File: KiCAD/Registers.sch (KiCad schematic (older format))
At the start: 25 parts, among them U701 74HCT138N, U704 74LS27, U705 74HCT32N, U706 74HCT574N, U707 74HCT574N, U708 74HCT574N, U712 74LS27, U713 74HCT32N, U714 74HCT574N, U715 74HCT574N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

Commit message: Moved SP out of register module into SP module; changed RS0 assert signal alias from RS0 to RSH; moved uCode and program code to different subdirs of Programming/ .
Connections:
- net REG_ASSERT_RS0 renamed RSH
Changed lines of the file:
@@
 $EndComp
 Text HLabel 1400 5050 0    50   Input ~ 0
-REG_ASSERT_RS0
+RSH
 Wire Wire Line
 	1400 4725 1450 4725

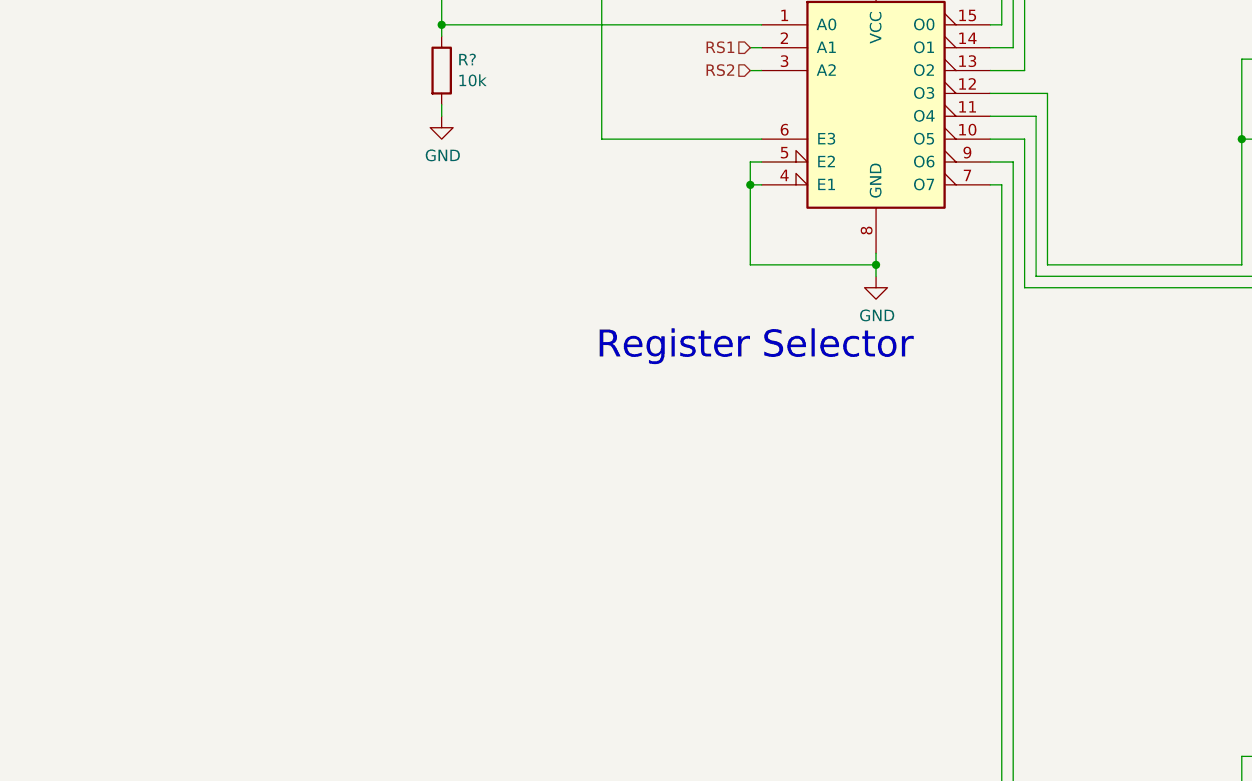
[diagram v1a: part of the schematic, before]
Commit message: First working versiongit add .  Added CSU control signal for updating C and O flags during add operations only.  Added circuitry to disable the reg decoder unless ~RI or ~RO are asserted.  Potential future issues: PC clock noise, reg clock noise, clock module being crap..
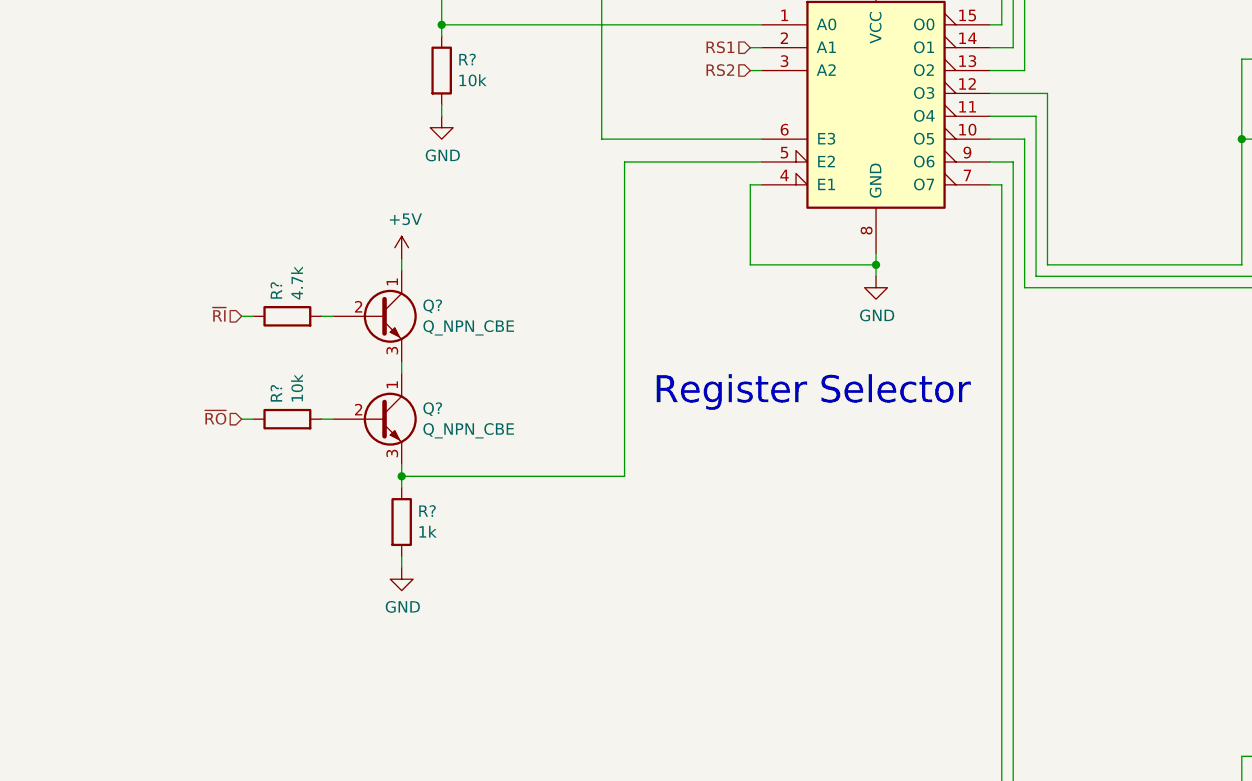
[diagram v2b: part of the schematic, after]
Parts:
- added Q? (x2): Q_NPN_CBE, symbol Breadboard_CPU-rescue:Q_NPN_CBE-Device
- added R?: 4.7k, symbol Breadboard_CPU-rescue:R-Device
- added R?: 10k, symbol Breadboard_CPU-rescue:R-Device
- added R?: 1k, symbol Breadboard_CPU-rescue:R-Device
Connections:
- net +5V: now also Q?.1 (C)
- net GND: now also R?.2; no longer U701.5 (E2)
- net ~RI: now also R?.1
- net ~RO: now also R?.1
- new net: Q?.3 (E), R?.1, U701.5 (E2)
- new net: Q?.2 (B), R?.2 (x2)
- new net: Q?.1 (C), Q?.3 (E)
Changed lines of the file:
@@
 Text Notes 12050 10350 0    118  ~ 0
 Register file
-Text Notes 2475 6700 0    118  ~ 0
+Text Notes 2725 6900 0    118  ~ 0
 Register Selector
 $Comp
@@
 Wire Wire Line
 	3150 5925 3150 6275
-Connection ~ 3150 5925
 Wire Wire Line
 	3200 5925 3150 5925
 Wire Wire Line
 	3150 6275 3700 6275
-Wire Wire Line
-	3150 5825 3150 5925
-Wire Wire Line
-	3200 5825 3150 5825
 Wire Wire Line
 	2500 5725 2500 4875
@@
 	1    0    0    -1
 $EndComp
+Wire Wire Line
+	1625 7200 1625 7150
+Connection ~ 1625 7200
+Wire Wire Line
+	1625 7200 2600 7200
+$Comp
+L Breadboard_CPU-rescue:GND-power #PWR?
+U 1 1 60FC9E28
+P 1625 7600
+F 0 "#PWR?" H 1625 7350 50  0001 C CNN
+F 1 "GND" H 1630 7427 50  0000 C CNN
+F 2 "" H 1625 7600 50  0001 C CNN
+F 3 "" H 1625 7600 50  0001 C CNN
+	1    1625 7600
+	1    0    0    -1
+$EndComp
+Wire Wire Line
+	1625 7600 1625 7550
+Wire Wire Line
+	925  6500 975  6500
+Wire Wire Line
+	975  6950 925  6950
+Wire Wire Line
+	1275 6500 1325 6500
+$Comp
+L Breadboard_CPU-rescue:R-Device R?
+U 1 1 60FC9E32
+P 1125 6500
+AR Path="/5EFC06D4/60FC9E32" Ref="R?"  Part="1"
+AR Path="/5EFC04D0/60FC9E32" Ref="R?"  Part="1"
+F 0 "R?" H 1195 6546 50  0000 L CNN
+F 1 "4.7k" H 1195 6455 50  0000 L CNN
+F 2 "" V 1055 6500 50  0001 C CNN
+F 3 "~" H 1125 6500 50  0001 C CNN
+	1    1125 6500
+	0    -1   -1   0
+$EndComp
+Wire Wire Line
+	1275 6950 1325 6950
+$Comp
+L Breadboard_CPU-rescue:R-Device R?
+U 1 1 60FC9E39
+P 1125 6950
+F 0 "R?" H 1195 6996 50  0000 L CNN
+F 1 "10k" H 1195 6905 50  0000 L CNN
+F 2 "" V 1055 6950 50  0001 C CNN
+F 3 "~" H 1125 6950 50  0001 C CNN
+	1    1125 6950
+	0    -1   -1   0
+$EndComp
+$Comp
+L Breadboard_CPU-rescue:R-Device R?
+U 1 1 60FC9E3F
+P 1625 7400
+F 0 "R?" H 1695 7446 50  0000 L CNN
+F 1 "1k" H 1695 7355 50  0000 L CNN
+F 2 "" V 1555 7400 50  0001 C CNN
+F 3 "~" H 1625 7400 50  0001 C CNN
+	1    1625 7400
+	1    0    0    -1
+$EndComp
+Wire Wire Line
+	1625 6250 1625 6300
+Wire Wire Line
+	1625 7250 1625 7200
+Wire Wire Line
+	1625 6750 1625 6700
+$Comp
+L Breadboard_CPU-rescue:Q_NPN_CBE-Device Q?
+U 1 1 60FC9E48
+P 1525 6950
+F 0 "Q?" H 1716 6996 50  0000 L CNN
+F 1 "Q_NPN_CBE" H 1716 6905 50  0000 L CNN
+F 2 "" H 1725 7050 50  0001 C CNN
+F 3 "~" H 1525 6950 50  0001 C CNN
+	1    1525 6950
+	1    0    0    -1
+$EndComp
+$Comp
+L Breadboard_CPU-rescue:Q_NPN_CBE-Device Q?
+U 1 1 60FC9E4E
+P 1525 6500
+F 0 "Q?" H 1716 6546 50  0000 L CNN
+F 1 "Q_NPN_CBE" H 1716 6455 50  0000 L CNN
+F 2 "" H 1725 6600 50  0001 C CNN
+F 3 "~" H 1525 6500 50  0001 C CNN
+	1    1525 6500
+	1    0    0    -1
+$EndComp
+$Comp
+L power:+5V #PWR?
+U 1 1 60FC9E54
+P 1625 6250
+AR Path="/5F05F116/60FC9E54" Ref="#PWR?"  Part="1"
+AR Path="/5EFC06D4/60FC9E54" Ref="#PWR?"  Part="1"
+F 0 "#PWR?" H 1625 6100 50  0001 C CNN
+F 1 "+5V" H 1640 6423 50  0000 C CNN
+F 2 "" H 1625 6250 50  0001 C CNN
+F 3 "" H 1625 6250 50  0001 C CNN
+	1    1625 6250
+	1    0    0    -1
+$EndComp
+Text HLabel 925  6950 0    50   Input ~ 0
+~RO
+Text HLabel 925  6500 0    50   Input ~ 0
+~RI
+Wire Wire Line
+	2600 7200 2600 5825
+Wire Wire Line
+	2600 5825 3200 5825
 $EndSCHEMATC
